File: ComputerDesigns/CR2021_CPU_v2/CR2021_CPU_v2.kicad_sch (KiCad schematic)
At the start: 30 parts, among them SW1 RESET, U3 7400, U4 7400

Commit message: add sound
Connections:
- net DATA0: now reaches BUS1.1 (Pin_1), CPU1.33 (D0), IN1.18 (Y0), IN2.18 (Y0), OUT1.3 (D0), OUT2.3 (D0), RAM1.11 (Q0), ROM1.11 (D0)
- net DATA1: now reaches BUS1.2 (Pin_2), CPU1.32 (D1), IN1.17 (Y1), IN2.17 (Y1), OUT1.4 (D1), OUT2.4 (D1), RAM1.12 (Q1), ROM1.12 (D1)
- net DATA2: now reaches BUS1.3 (Pin_3), CPU1.31 (D2), IN1.16 (Y2), IN2.16 (Y2), OUT1.7 (D2), OUT2.7 (D2), RAM1.13 (Q2), ROM1.13 (D2)
- net DATA3: now reaches BUS1.4 (Pin_4), CPU1.30 (D3), IN1.15 (Y3), IN2.15 (Y3), OUT1.8 (D3), OUT2.8 (D3), RAM1.15 (Q3), ROM1.15 (D3)
- net DATA4: now reaches BUS1.5 (Pin_5), CPU1.29 (D4), IN1.14 (Y4), IN2.14 (Y4), OUT1.13 (D4), OUT2.13 (D4), RAM1.16 (Q4), ROM1.16 (D4)
- net DATA5: now reaches BUS1.6 (Pin_6), CPU1.28 (D5), IN1.13 (Y5), IN2.13 (Y5), OUT1.14 (D5), OUT2.14 (D5), RAM1.17 (Q5), ROM1.17 (D5)
- net DATA6: now reaches BUS1.7 (Pin_7), CPU1.27 (D6), IN1.12 (Y6), IN2.12 (Y6), OUT1.17 (D6), OUT2.17 (D6), RAM1.18 (Q6), ROM1.18 (D6)
- net DATA7: now reaches BUS1.8 (Pin_8), CPU1.26 (D7), IN1.11 (Y7), IN2.11 (Y7), OUT1.18 (D7), OUT2.18 (D7), RAM1.19 (Q7), ROM1.19 (D7)
- net $4001_IN: now reaches IN2.1 (G1), IN_DEMUX1.14 (O1)
- net $4000_IN: now reaches IN1.1 (G1), IN_DEMUX1.15 (O0)
- net $4001_OUT: now reaches OUT2.11 (Cp), OUT_DEMUX1.14 (O1)
- net $4003_OUT: now reaches CONN8.2 (Pin_2), OUT_DEMUX1.12 (O3)
- net $4002_OUT: now reaches CONN8.1 (Pin_1), OUT_DEMUX1.13 (O2)
- net $4000_OUT: now reaches OUT1.11 (Cp), OUT_DEMUX1.15 (O0)
- net R!W renamed R/!W
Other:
- sheet clock circuit renamed Clock
- note added: "Possibly add pulldown/up resistors here? Make it a "JOYSTICK PORT""
- moved on the sheet: CONN8, PIN1

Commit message: update schematics
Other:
- added sheet 6522_IO (6522.kicad_sch)
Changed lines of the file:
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@@
 	(wire
 		(pts
-			(xy 191.77 109.22) (xy 191.77 147.32)
-		)
-		(stroke
-			(width 0)
-			(type default)
-		)
-	)
-	(wire
-		(pts
 			(xy 54.61 140.97) (xy 76.2 140.97)
 		)
@@
 	(wire
 		(pts
+			(xy 191.77 109.22) (xy 191.77 147.32)
+		)
+		(stroke
+			(width 0)
+			(type default)
+		)
+	)
+	(wire
+		(pts
 			(xy 201.93 83.82) (xy 218.44 83.82)
 		)
@@
 	)
 	(label "R!W"
-		(at 191.77 146.05 0)
+		(at 191.77 147.32 0)
 		(effects
 			(font
@@
 				)
 			)
+		)
+	)
+	(sheet
+		(at 25.4 255.27)
+		(size 12.7 3.81)
+		(exclude_from_sim no)
+		(in_bom yes)
+		(on_board yes)
+		(dnp no)
+		(fields_autoplaced yes)
+		(stroke
+			(width 0.1524)
+			(type solid)
+		)
+		(fill
+			(color 0 0 0 0.0000)
+		)
+		(property "Sheetname" "6522_IO"
+			(at 25.4 254.5584 0)
+			(effects
+				(font
+					(size 1.27 1.27)
+				)
+				(justify left bottom)
+			)
+		)
+		(property "Sheetfile" "6522.kicad_sch"
+			(at 25.4 259.6646 0)
+			(effects
+				(font
+					(size 1.27 1.27)
+				)
+				(justify left top)
+			)
+		)
+		(instances
+			(project "CR2021_CPU_v2"
+				(path "/5ba384c5-5050-42b4-8e60-2da7b065216b"
+					(page "4")
+				)
+			)

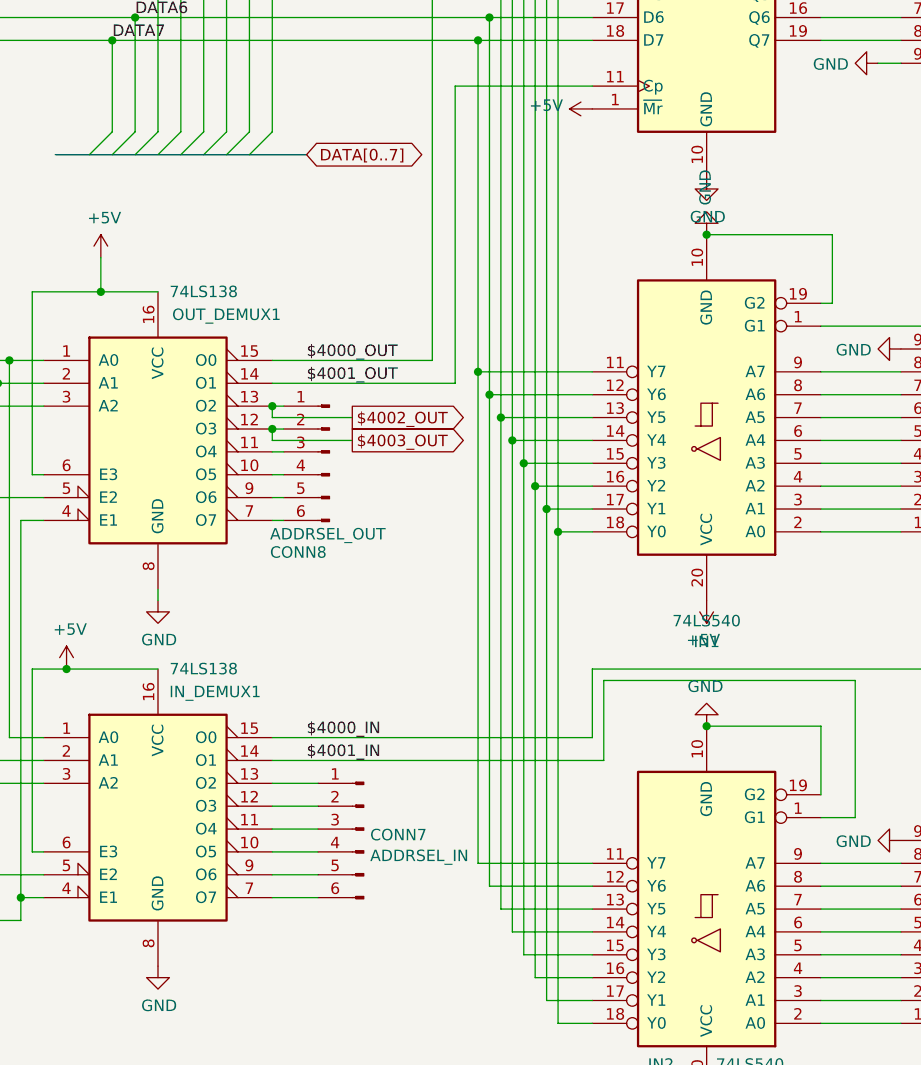
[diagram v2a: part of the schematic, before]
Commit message: add some VIA addresses
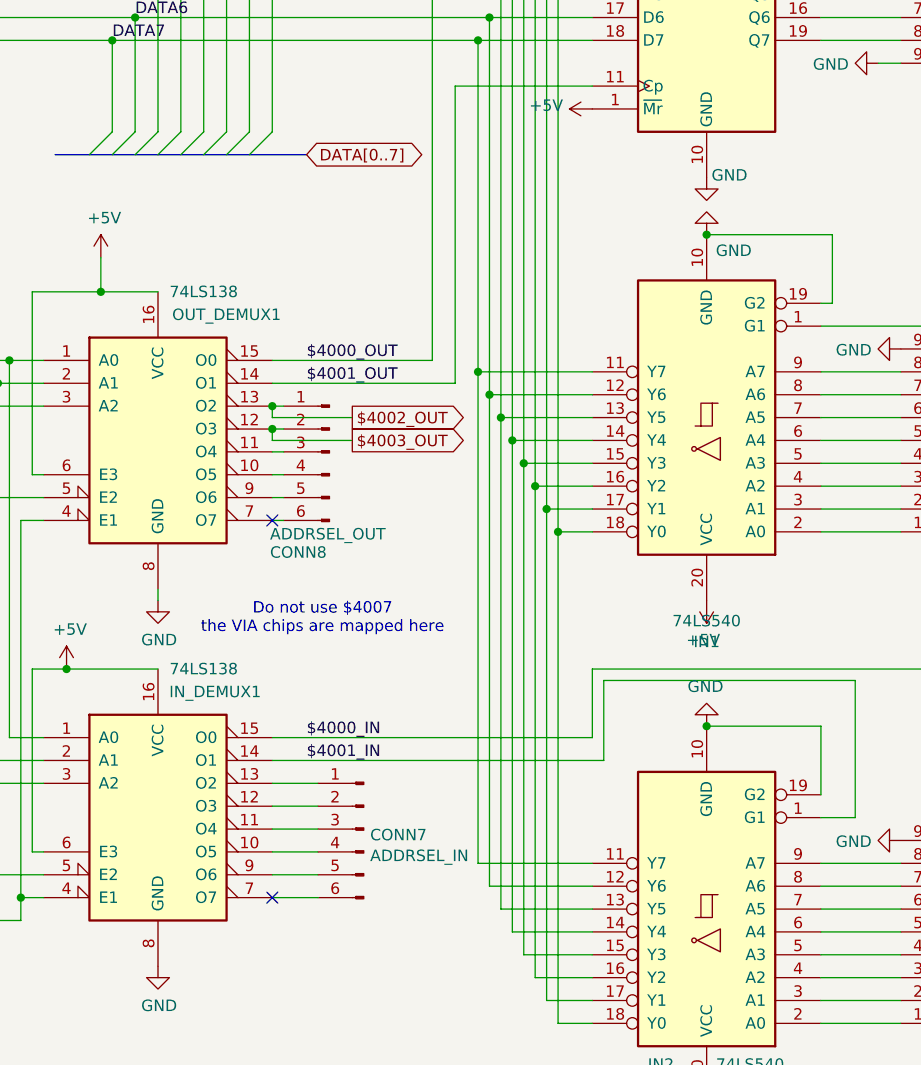
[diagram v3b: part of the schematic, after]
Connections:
- no-connect marks 11 -> 13
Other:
- note added: "Do not use $4007 the VIA chips are mapped here"
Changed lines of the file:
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@@
 		)
 	)
+	(text "Do not use $4007\nthe VIA chips are mapped here"
+		(exclude_from_sim no)
+		(at 265.938 155.702 0)
+		(effects
+			(font
+				(size 1.27 1.27)
+			)
+		)
+	)
 	(text "Possibly add pulldown/up resistors here?\nMake it a \"JOYSTICK PORT\""
 		(exclude_from_sim no)
@@
 	)
 	(no_connect
+		(at 260.35 186.69)
+	)
+	(no_connect
+		(at 260.35 144.78)
+	)
+	(no_connect
 		(at 156.21 66.04)
 	)
@@
 		)
 		(property "Value" "GND"
-			(at 308.737 111.0742 0)
+			(at 311.15 106.426 0)
 			(effects
 				(font
@@
 		)
 		(property "Value" "GND"
-			(at 308.483 109.7788 90)
+			(at 309.626 114.808 0)
 			(effects
 				(font
